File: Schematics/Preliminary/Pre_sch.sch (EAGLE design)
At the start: 39 parts, among them IC1 7805TV, IC2 7805TV, J1 3x2 M, J2 1x6 M, SW1 !RESET, SW2 Unlock, U2 A4988_STEPPER_MOTOR_DRIVER_CA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, U4 ATMEGA328P-PU, X1 16 MHz

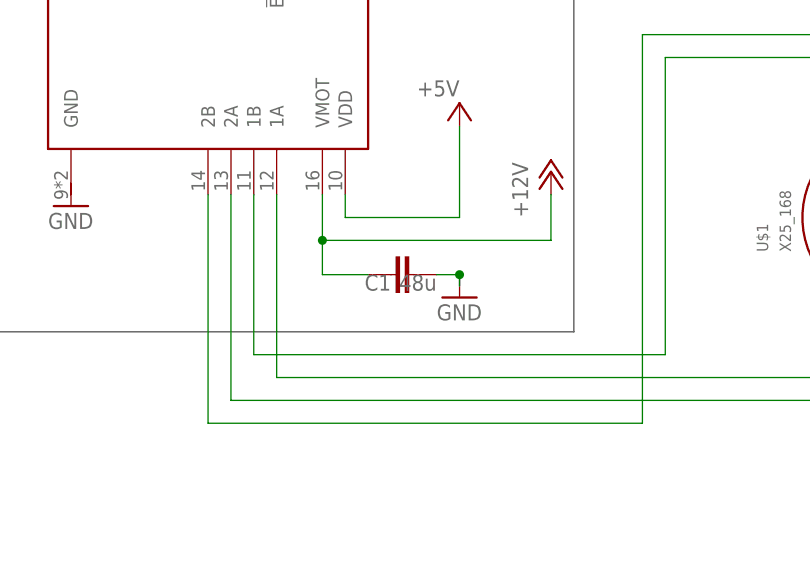
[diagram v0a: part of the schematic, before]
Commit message: Preliminary Board Layout is done
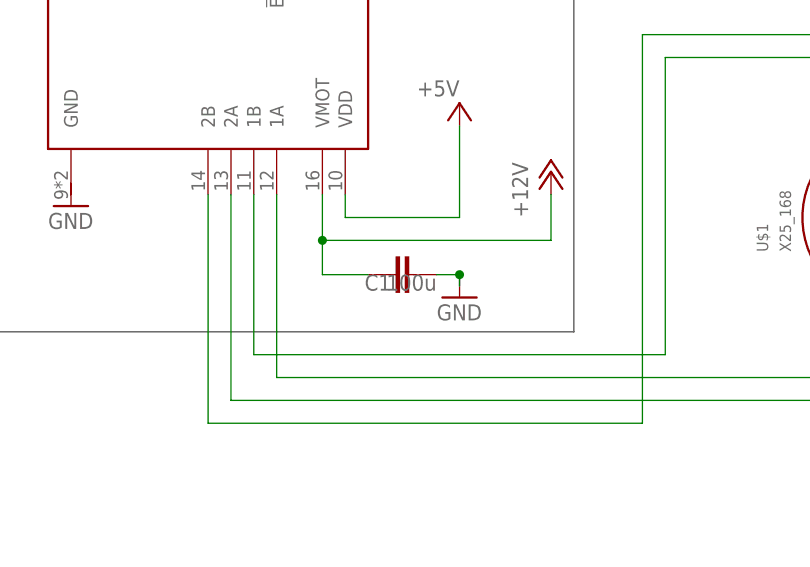
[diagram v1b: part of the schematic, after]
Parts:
- C1: value 48u -> 100u
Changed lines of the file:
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@@
 <part name="P+6" library="supply1" library_urn="urn:adsk.eagle:library:371" deviceset="+12V" device=""/>
 <part name="P+8" library="supply1" library_urn="urn:adsk.eagle:library:371" deviceset="+12V" device=""/>
-<part name="C1" library="rcl" library_urn="urn:adsk.eagle:library:334" deviceset="C-EU" device="C0805K" package3d_urn="urn:adsk.eagle:package:23681/2" value="48u">
+<part name="C1" library="rcl" library_urn="urn:adsk.eagle:library:334" deviceset="C-EU" device="C0805K" package3d_urn="urn:adsk.eagle:package:23681/2" value="100u">
 <spice>
 <pinmapping spiceprefix="C">
